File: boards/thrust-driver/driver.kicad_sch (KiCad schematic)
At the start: 25 parts, among them J1 HELM J13 1:1, J2 LUG BATT+, J3 LUG BATT-, J4 LUG MOT A, J5 LUG MOT B, U1 BTN8982TA, U2 BTN8982TA, U3 BTN8982TA, U4 BTN8982TA

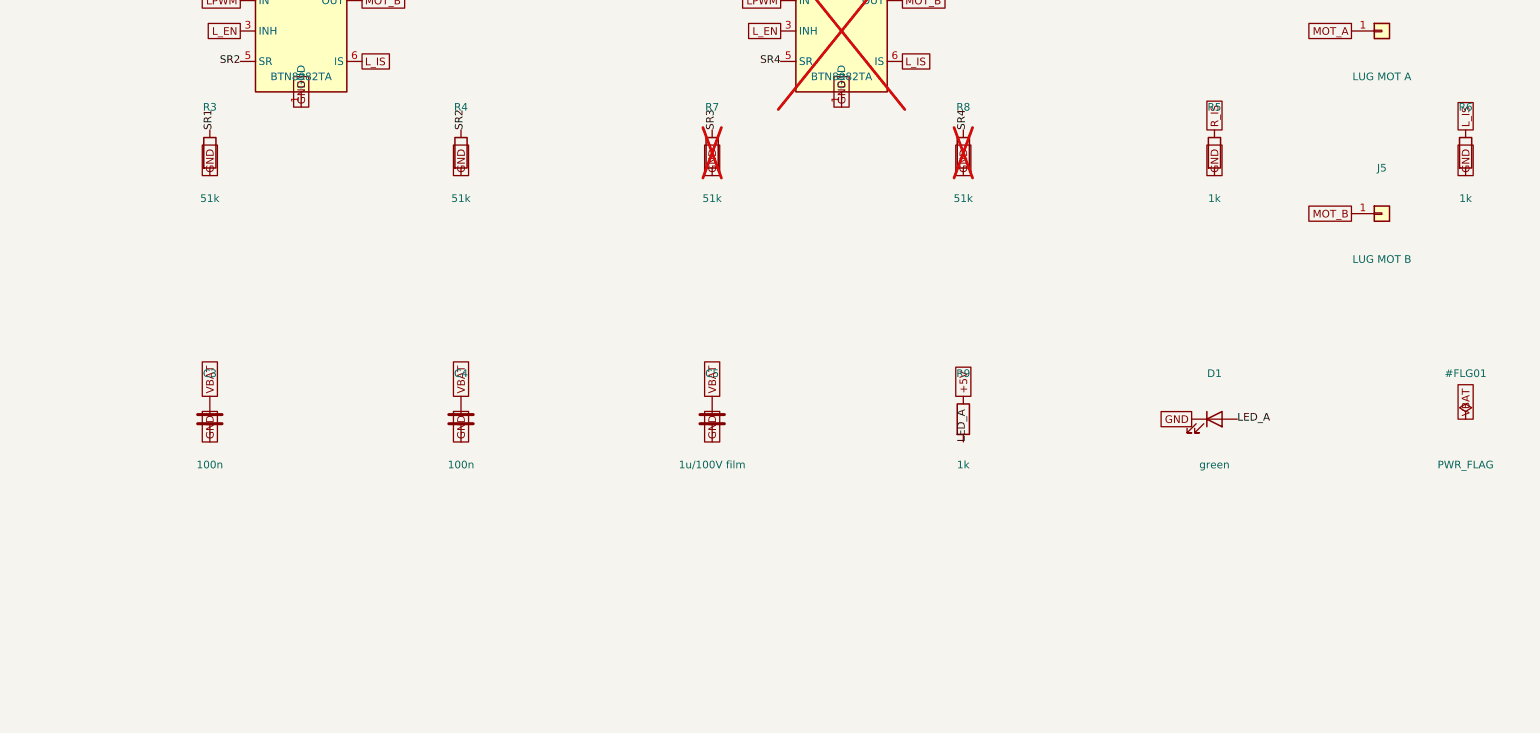
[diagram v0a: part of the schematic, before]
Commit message: feat(thrust-driver): NMEA2000 smart-node provision — DNP Pico 2 + CAN/N2K connectors, board 95x92
Unpopulated through-hole provision to run the bridge as a standalone N2K
node: U5 Pico 2 (GP12-15 parallel to J1 drive nets, GP26/27 ADC sense via
R12/R13 1k, GP18/19 CAN), U6 SIP-3 5V reg from VBAT, J6 transceiver
header (3V3/GND/TX/RX), J7 N2K V+/GND/SHIELD with 0R power-tap/shield
options. Board grew 75->92mm; existing routing untouched; DRC 0 errors /
0 unconnected (solder-lane mask apertures set to ignore by design).

Co-Authored-By: Claude Fable 5 <noreply@anthropic.com>
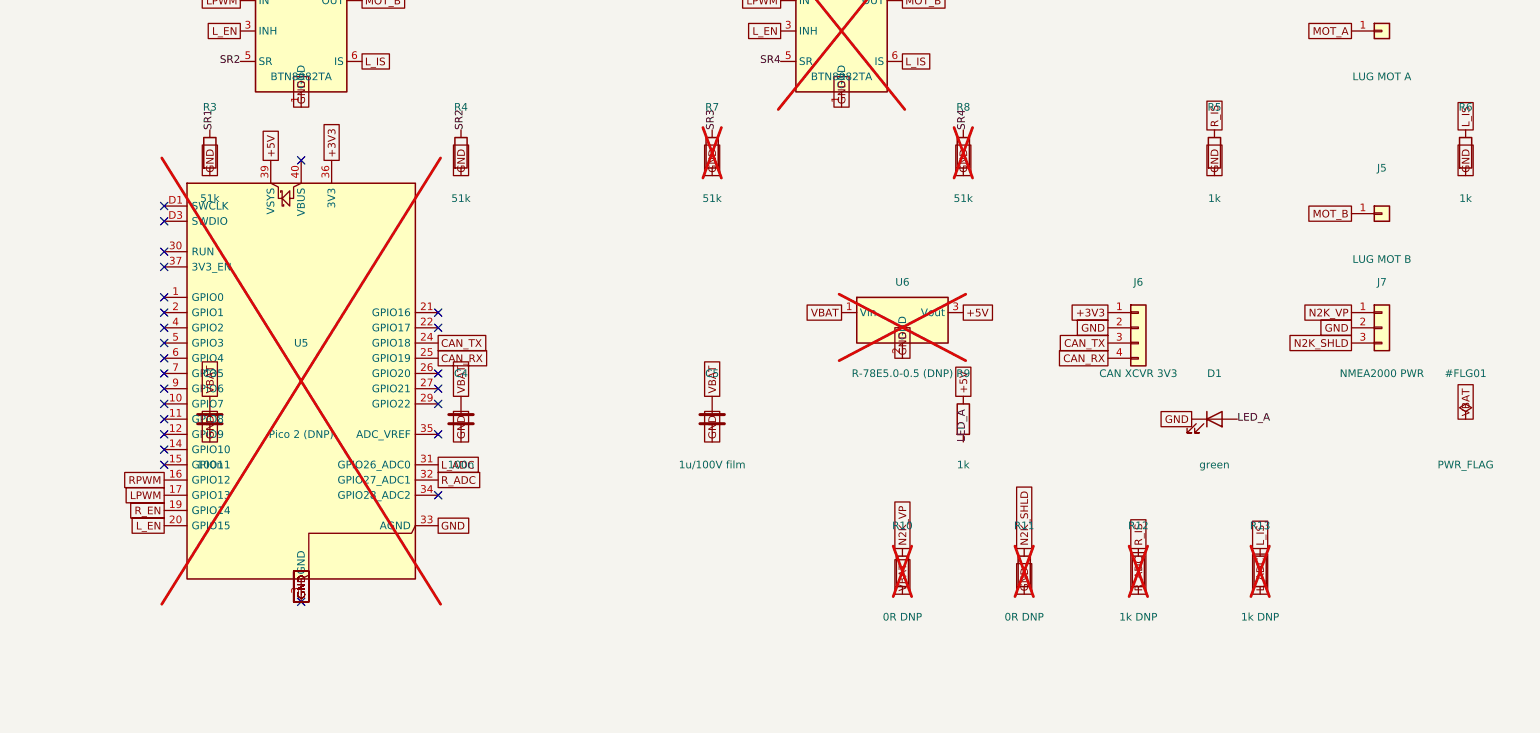
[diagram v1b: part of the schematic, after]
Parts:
- added J6: CAN XCVR 3V3, Connector_PinHeader_2.54mm:PinHeader_1x04_P2.54mm_Vertical, symbol Connector_Generic:Conn_01x04
- added J7: NMEA2000 PWR, Connector_JST:JST_XH_B3B-XH-A_1x03_P2.50mm_Vertical, symbol Connector_Generic:Conn_01x03
- added R10, R11: 0R DNP, Resistor_SMD:R_0805_2012Metric, symbol Device:R
- added R12, R13: 1k DNP, Resistor_SMD:R_0805_2012Metric, symbol Device:R
- added U5: Pico 2 (DNP), vanchor-helm:RaspberryPi_Pico_TH_SWD, symbol MCU_Module:RaspberryPi_Pico_Debug
- added U6: R-78E5.0-0.5 (DNP), Converter_DCDC:Converter_DCDC_TRACO_TSR-1_THT, symbol Converter_DCDC:TSR_1-2450
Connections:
- net +5V: now also U5.39 (VSYS), U6.3 (Vout)
- net GND: now also J6.2 (Pin_2), J7.2 (Pin_2), R11.2, U5.13 (GND), U5.18 (GND), U5.23 (GND), U5.28 (GND), U5.3 (GND), U5.33 (AGND), U5.38 (GND), U5.8 (GND), U5.D2 (GND), U6.2 (GND)
- net LPWM: now also U5.17 (GPIO13)
- net L_EN: now also U5.20 (GPIO15)
- net L_IS: now also R13.1
- net RPWM: now also U5.16 (GPIO12)
- net R_EN: now also U5.19 (GPIO14)
- net R_IS: now also R12.1
- net VBAT: now also R10.2, U6.1 (Vin)
- new net +3V3: J6.1 (Pin_1), U5.36 (3V3)
- new net CAN_RX: J6.4 (Pin_4), U5.25 (GPIO19)
- new net CAN_TX: J6.3 (Pin_3), U5.24 (GPIO18)
- new net L_ADC: R13.2, U5.31 (GPIO26_ADC0)
- new net N2K_SHLD: J7.3 (Pin_3), R11.1
- new net N2K_VP: J7.1 (Pin_1), R10.1
- new net R_ADC: R12.2, U5.32 (GPIO27_ADC1)
- no-connect marks 0 -> 25
